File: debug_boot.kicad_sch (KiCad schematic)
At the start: 0 parts

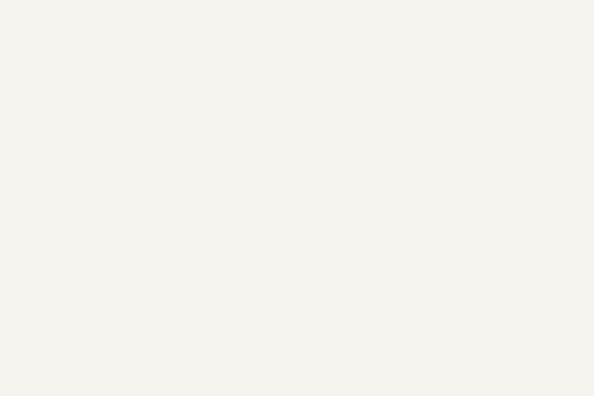
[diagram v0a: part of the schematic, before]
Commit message: Use local labels for RGB bus in folio and add title for all folio
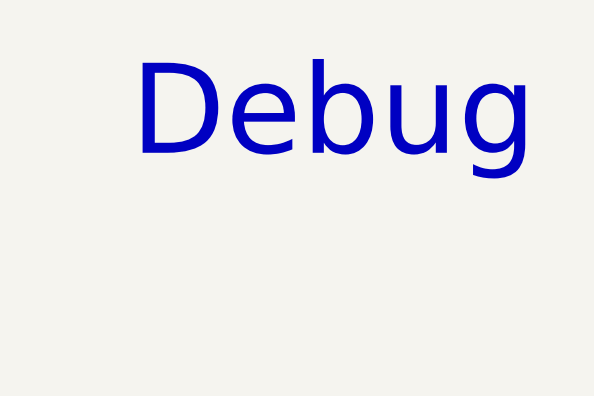
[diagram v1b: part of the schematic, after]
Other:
- note added: "Debug"
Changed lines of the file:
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@@
 	(generator_version "9.0")
 	(paper "A4")
+	(text "Debug"
+		(exclude_from_sim no)
+		(at 151.892 25.146 0)
+		(effects
+			(font
+				(size 10 10)
+			)
+		)
+	)
 	(hierarchical_label "~{SS}_Debug"
 		(shape output)

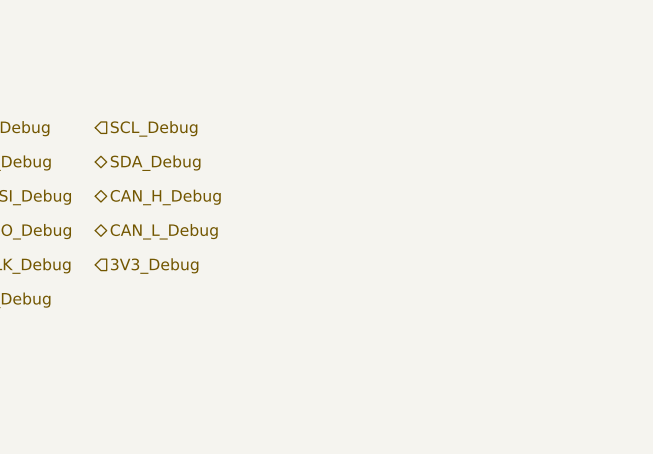
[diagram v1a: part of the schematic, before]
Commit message: Add SWG ARM/JTAG connector 10 pins
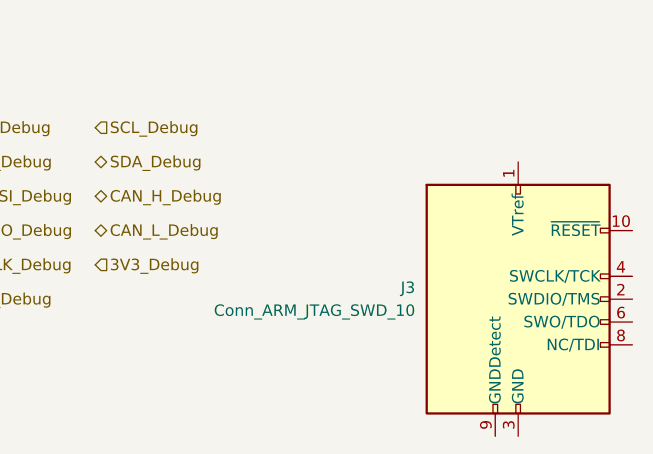
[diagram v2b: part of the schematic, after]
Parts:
- added J3: Conn_ARM_JTAG_SWD_10, Connector_PinHeader_1.27mm:PinHeader_2x05_P1.27mm_Vertical_SMD, symbol Connector:Conn_ARM_JTAG_SWD_10
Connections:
- new net: J3.3 (GND), J3.5 (GND)
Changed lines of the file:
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@@
+		)
+	)
+	(symbol
+		(lib_id "Connector:Conn_ARM_JTAG_SWD_10")
+		(at 179.07 85.09 0)
+		(unit 1)
+		(exclude_from_sim no)
+		(in_bom yes)
+		(on_board yes)
+		(dnp no)
+		(fields_autoplaced yes)
+		(property "Reference" "J3"
+			(at 167.64 83.8199 0)
+			(effects
+				(font
+					(size 1.27 1.27)
+				)
+				(justify right)
+			)
+		)
+		(property "Value" "Conn_ARM_JTAG_SWD_10"
+			(at 167.64 86.3599 0)
+			(effects
+				(font
+					(size 1.27 1.27)
+				)
+				(justify right)
+			)
+		)
+		(property "Footprint" "Connector_PinHeader_1.27mm:PinHeader_2x05_P1.27mm_Vertical_SMD"
+			(at 179.07 85.09 0)
+			(effects
+				(font
+					(size 1.27 1.27)
+				)
+				(hide yes)
+			)
+		)
+		(property "Datasheet" "http://infocenter.arm.com/help/topic/com.arm.doc.ddi0314h/DDI0314H_coresight_components_trm.pdf"
+			(at 170.18 116.84 90)
+			(effects
+				(font
+					(size 1.27 1.27)
+				)
+				(hide yes)
+			)
+		)
+		(property "Description" "Cortex Debug Connector, standard ARM Cortex-M SWD and JTAG interface"
+			(at 179.07 85.09 0)
+			(effects
+				(font
+					(size 1.27 1.27)
+				)
+				(hide yes)
+			)
+		)
+		(pin "1"
+		)
+		(pin "7"
+		)
+		(pin "8"
+		)
+		(pin "10"
+		)
+		(pin "5"
+		)
+		(pin "4"
+		)
+		(pin "6"
+		)
+		(pin "9"
+		)
+		(pin "3"
+		)
+		(pin "2"
+		)
+		(instances
+			(project "weather-station-poc"
+				(path "/38eb53bb-294e-46e4-ad59-fd355ca373b9/8a588a02-5ba4-4712-b770-7d9eb4e5d127"
+					(reference "J3")
+					(unit 1)
+				)
+			)
 		)
 	)

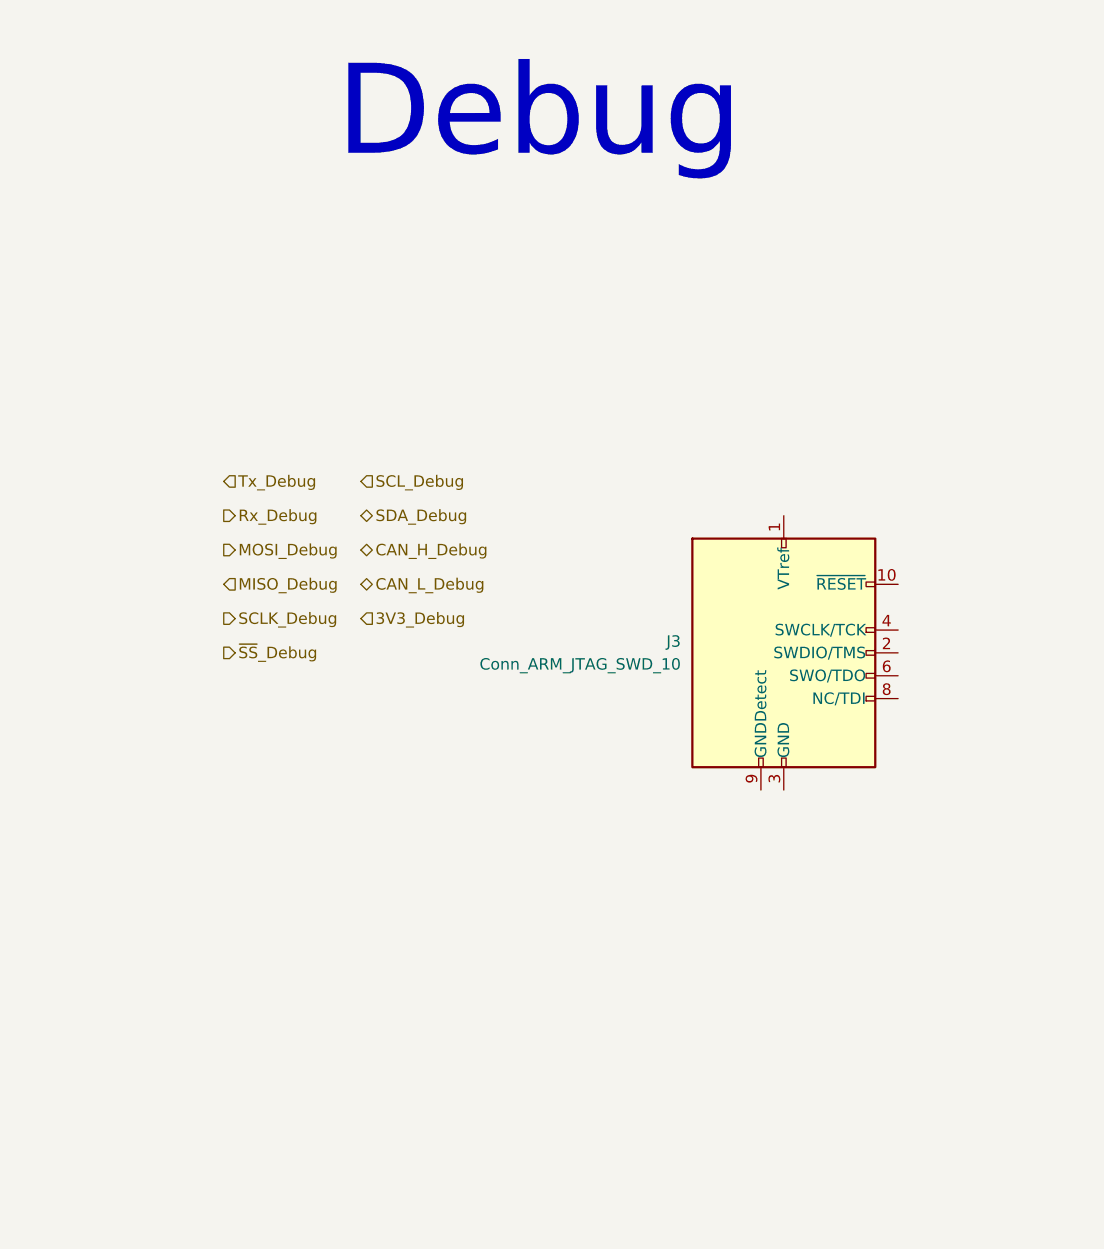
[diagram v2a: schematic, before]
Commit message: Add debug connectors
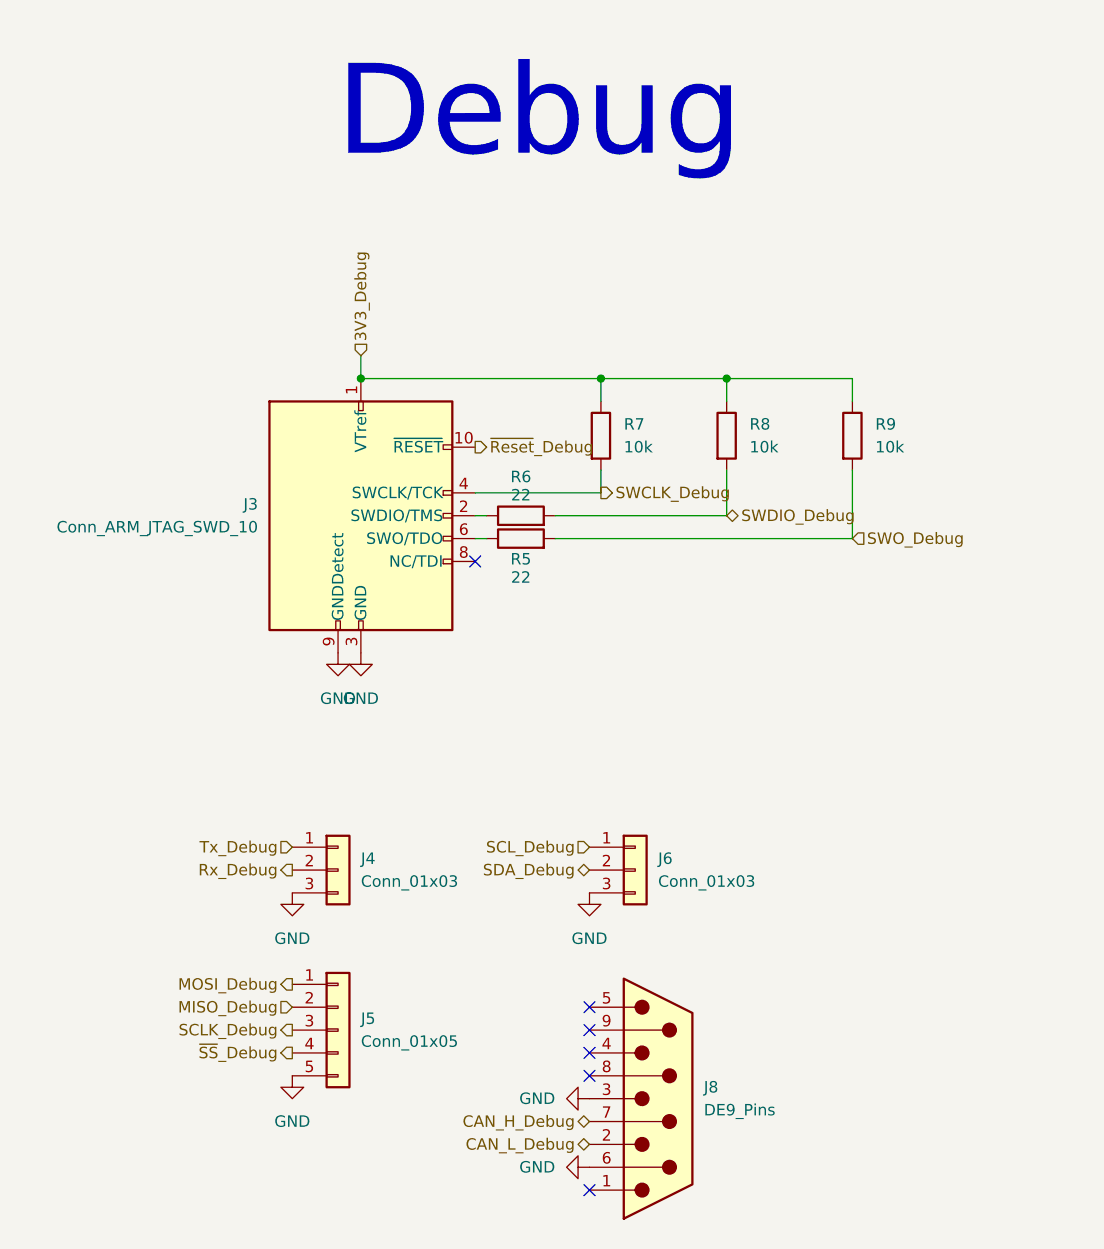
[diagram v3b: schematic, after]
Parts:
- added J4, J6: Conn_01x03, symbol Connector_Generic:Conn_01x03
- added J5: Conn_01x05, symbol Connector_Generic:Conn_01x05
- added J8: DE9_Pins, symbol Connector:DE9_Pins
- added R5, R6: 22, symbol Device:R
- added R7, R8, R9: 10k, symbol Device:R
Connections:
- net 3V3_Debug: now also J3.1 (VTref), R7.1, R8.1, R9.1
- net CAN_H_Debug: now also J8.7
- net CAN_L_Debug: now also J8.2
- net MISO_Debug: now also J5.2 (Pin_2)
- net MOSI_Debug: now also J5.1 (Pin_1)
- net Rx_Debug: now also J4.2 (Pin_2)
- net SCLK_Debug: now also J5.3 (Pin_3)
- net SCL_Debug: now also J6.1 (Pin_1)
- net SDA_Debug: now also J6.2 (Pin_2)
- net Tx_Debug: now also J4.1 (Pin_1)
- net ~{SS}_Debug: now also J5.4 (Pin_4)
- net ~{Reset}_Debug: now reaches J3.10 (~{RESET})
- net at J3.2 (SWDIO/TMS): now also R6.1
- net GND: now reaches J3.3 (GND), J3.5 (GND)
- net GND: now also J3.9 (GNDDetect), J4.3 (Pin_3), J5.5 (Pin_5), J6.3 (Pin_3), J8.3, J8.6
- net SWCLK_Debug: now reaches J3.4 (SWCLK/TCK)
- net SWCLK_Debug: now also R7.2
- net at J3.6 (SWO/TDO): now also R5.1
- new net SWDIO_Debug: R6.2, R8.2
- new net SWO_Debug: R5.2, R9.2
- no-connect marks 0 -> 6
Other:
- moved on the sheet: J3

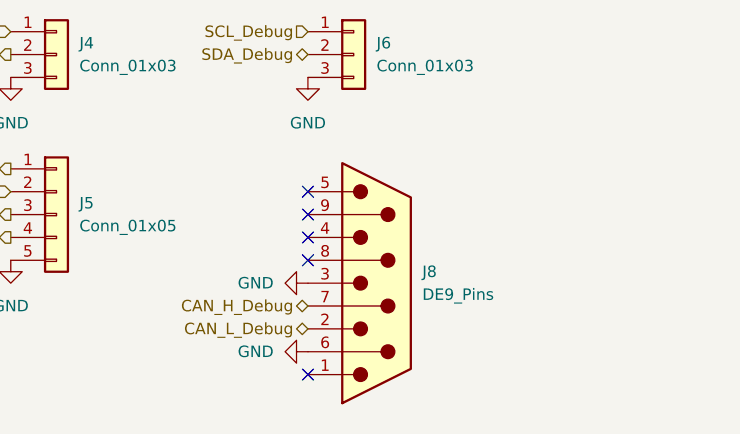
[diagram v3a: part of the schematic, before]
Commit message: Cable all sensors
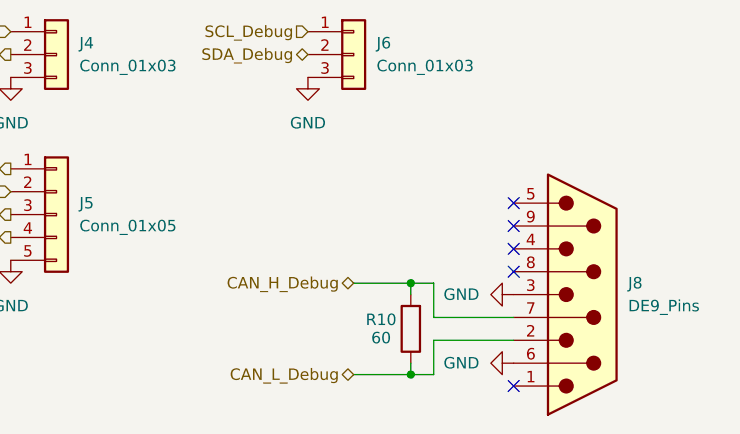
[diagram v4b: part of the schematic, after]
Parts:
- added R10: 60, symbol Device:R
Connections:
- net CAN_H_Debug: now also R10.2
- net CAN_L_Debug: now also R10.1
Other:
- moved on the sheet: J8
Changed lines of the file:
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@@
+	)
+	(junction
+		(at 168.91 144.78)
+		(diameter 0)
+		(color 0 0 0 0)
+	)
+	(junction
+		(at 168.91 134.62)
+		(diameter 0)
+		(color 0 0 0 0)
 	)
 	(junction
@@
 	)
 	(no_connect
-		(at 157.48 124.46)
+		(at 180.34 125.73)
 	)
 	(no_connect
-		(at 157.48 144.78)
+		(at 180.34 146.05)
 	)
 	(no_connect
@@
 	)
 	(no_connect
-		(at 157.48 132.08)
+		(at 180.34 133.35)
 	)
 	(no_connect
-		(at 157.48 127)
+		(at 180.34 128.27)
 	)
 	(no_connect
-		(at 157.48 129.54)
+		(at 180.34 130.81)
 	)
 	(wire
@@
 	(wire
 		(pts
+			(xy 162.56 144.78) (xy 168.91 144.78)
+		)
+		(stroke
+			(width 0)
+			(type default)
+		)
+	)
+	(wire
+		(pts
 			(xy 158.75 64.77) (xy 158.75 67.31)
 		)
@@
 	(wire
 		(pts
+			(xy 168.91 144.78) (xy 171.45 144.78)
+		)
+		(stroke
+			(width 0)
+			(type default)
+		)
+	)
+	(wire
+		(pts
+			(xy 168.91 143.51) (xy 168.91 144.78)
+		)
+		(stroke
+			(width 0)
+			(type default)
+		)
+	)
+	(wire
+		(pts
+			(xy 162.56 134.62) (xy 168.91 134.62)
+		)
+		(stroke
+			(width 0)
+			(type default)
+		)
+	)
+	(wire
+		(pts
 			(xy 132.08 52.07) (xy 132.08 54.61)
 		)
@@
 	(wire
 		(pts
+			(xy 171.45 138.43) (xy 180.34 138.43)
+		)
+		(stroke
+			(width 0)
+			(type default)
+		)
+	)
+	(wire
+		(pts
 			(xy 172.72 54.61) (xy 186.69 54.61)
 		)
@@
 	(wire
 		(pts
+			(xy 171.45 144.78) (xy 171.45 140.97)
+		)
+		(stroke
+			(width 0)
+			(type default)
+		)
+	)
+	(wire
+		(pts
 			(xy 132.08 54.61) (xy 158.75 54.61)
 		)
@@
 	(wire
 		(pts
+			(xy 171.45 140.97) (xy 180.34 140.97)
+		)
+		(stroke
+			(width 0)
+			(type default)
+		)
+	)
+	(wire
+		(pts
 			(xy 186.69 57.15) (xy 186.69 54.61)
 		)
@@
 	(wire
 		(pts
+			(xy 168.91 134.62) (xy 168.91 135.89)
+		)
+		(stroke
+			(width 0)
+			(type default)
+		)
+	)
+	(wire
+		(pts
+			(xy 171.45 134.62) (xy 171.45 138.43)
+		)
+		(stroke
+			(width 0)
+			(type default)
+		)
+	)
+	(wire
+		(pts
 			(xy 146.05 72.39) (xy 144.78 72.39)
 		)
@@
 		(pts
 			(xy 153.67 72.39) (xy 186.69 72.39)
+		)
+		(stroke
+			(width 0)
+			(type default)
+		)
+	)
+	(wire
+		(pts
+			(xy 168.91 134.62) (xy 171.45 134.62)
 		)
 		(stroke
@@
 	(hierarchical_label "CAN_H_Debug"
 		(shape bidirectional)
-		(at 157.48 137.16 180)
+		(at 162.56 134.62 180)
 		(effects
 			(font
@@
 	(hierarchical_label "CAN_L_Debug"
 		(shape bidirectional)
-		(at 157.48 139.7 180)
+		(at 162.56 144.78 180)
 		(effects
 			(font
@@
 	(symbol
 		(lib_id "power:GND")
-		(at 157.48 142.24 270)
+		(at 180.34 143.51 270)
 		(unit 1)
 		(exclude_from_sim no)
@@
 		(fields_autoplaced yes)
 		(property "Reference" "#PWR034"
-			(at 151.13 142.24 0)
+			(at 173.99 143.51 0)
 			(effects
 				(font
@@
 		)
 		(property "Value" "GND"
-			(at 153.67 142.2399 90)
+			(at 176.53 143.5099 90)
 			(effects
 				(font
@@
 		)
 		(property "Footprint" ""
-			(at 157.48 142.24 0)
+			(at 180.34 143.51 0)
 			(effects
 				(font
@@
 		)
 		(property "Datasheet" ""
-			(at 157.48 142.24 0)
+			(at 180.34 143.51 0)
 			(effects
 				(font
@@
 		)
 		(property "Description" "Power symbol creates a global label with name \"GND\" , ground"
-			(at 157.48 142.24 0)
+			(at 180.34 143.51 0)
 			(effects
 				(font
@@
 				(path "/38eb53bb-294e-46e4-ad59-fd355ca373b9/8a588a02-5ba4-4712-b770-7d9eb4e5d127"
 					(reference "#PWR034")
+					(unit 1)
+				)
+			)
+		)
+	)
+	(symbol
+		(lib_id "Device:R")
+		(at 168.91 139.7 180)
+		(unit 1)
+		(exclude_from_sim no)
+		(in_bom yes)
+		(on_board yes)
+		(dnp no)
+		(property "Reference" "R10"
+			(at 165.608 138.684 0)
+			(effects
+				(font
+					(size 1.27 1.27)
+				)
+			)
+		)
+		(property "Value" "60"
+			(at 165.608 140.716 0)
+			(effects
+				(font
+					(size 1.27 1.27)
+				)
+			)
+		)
+		(property "Footprint" ""
+			(at 170.688 139.7 90)
+			(effects
+				(font
+					(size 1.27 1.27)
+				)
+				(hide yes)
+			)
+		)
+		(property "Datasheet" "~"
+			(at 168.91 139.7 0)
+			(effects
+				(font
+					(size 1.27 1.27)
+				)
+				(hide yes)
+			)
+		)
+		(property "Description" "Resistor"
+			(at 168.91 139.7 0)
+			(effects
+				(font
+					(size 1.27 1.27)
+				)
+				(hide yes)
+			)
+		)
+		(pin "2"
+		)
+		(pin "1"
+		)
+		(instances
+			(project "weather-station-poc"
+				(path "/38eb53bb-294e-46e4-ad59-fd355ca373b9/8a588a02-5ba4-4712-b770-7d9eb4e5d127"
+					(reference "R10")
 					(unit 1)
 				)
@@
 	(symbol
 		(lib_id "power:GND")
-		(at 157.48 134.62 270)
+		(at 180.34 135.89 270)
 		(unit 1)
 		(exclude_from_sim no)
@@
 		(fields_autoplaced yes)
 		(property "Reference" "#PWR035"
-			(at 151.13 134.62 0)
+			(at 173.99 135.89 0)
 			(effects
 				(font
@@
 		)
 		(property "Value" "GND"
-			(at 153.67 134.6199 90)
+			(at 176.53 135.8899 90)
 			(effects
 				(font
@@
 		)
 		(property "Footprint" ""
-			(at 157.48 134.62 0)
+			(at 180.34 135.89 0)
 			(effects
 				(font
@@
 		)
 		(property "Datasheet" ""
-			(at 157.48 134.62 0)
+			(at 180.34 135.89 0)
 			(effects
 				(font
@@
 		)
 		(property "Description" "Power symbol creates a global label with name \"GND\" , ground"
-			(at 157.48 134.62 0)
+			(at 180.34 135.89 0)
 			(effects
 				(font
@@
 	(symbol
 		(lib_id "Connector:DE9_Pins")
-		(at 165.1 134.62 0)
+		(at 187.96 135.89 0)
 		(unit 1)
 		(exclude_from_sim no)
@@
 		(fields_autoplaced yes)
 		(property "Reference" "J8"
-			(at 170.18 133.3499 0)
+			(at 193.04 134.6199 0)
 			(effects
 				(font
@@
 		)
 		(property "Value" "DE9_Pins"
-			(at 170.18 135.8899 0)
+			(at 193.04 137.1599 0)
 			(effects
 				(font
@@
 		)
 		(property "Footprint" ""
-			(at 165.1 134.62 0)
+			(at 187.96 135.89 0)
 			(effects
 				(font
@@
 		)
 		(property "Datasheet" "~"
-			(at 165.1 134.62 0)
+			(at 187.96 135.89 0)
 			(effects
 				(font
@@
 		)
 		(property "Description" "9-pin D-SUB connector, pins (male)"
-			(at 165.1 134.62 0)
-			(effects
-				(font
+			(at 187.96 135.89 0)
+			(effects
+				(font
